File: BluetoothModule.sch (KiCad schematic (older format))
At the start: 15 parts, among them J8 SW_DIP_x01, U17 BM83SM1-00TA

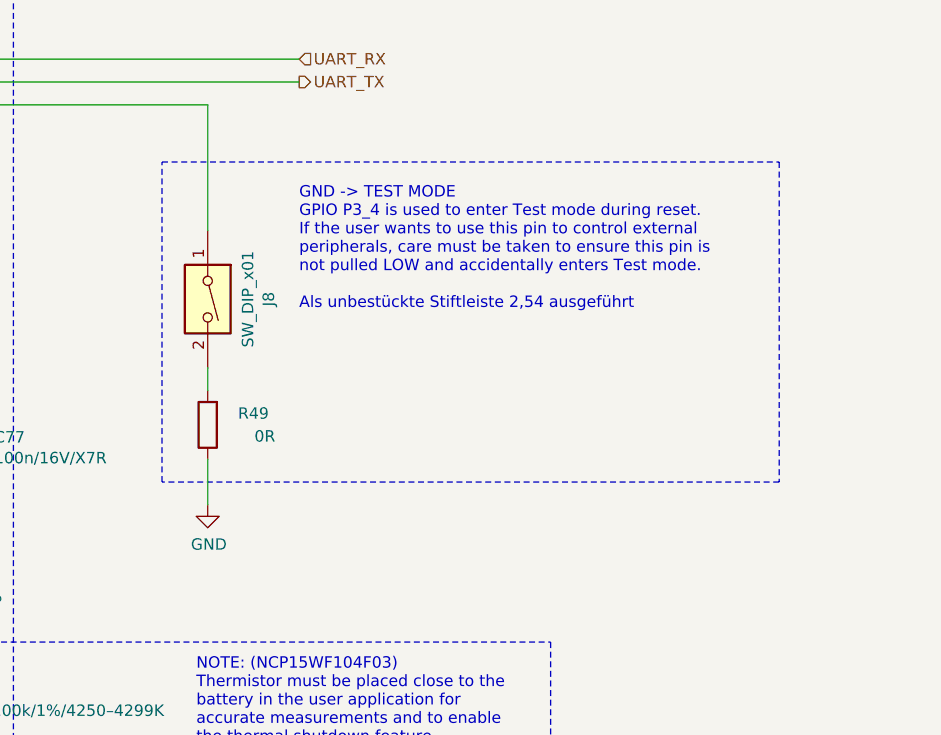
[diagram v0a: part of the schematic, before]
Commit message: - 1,5mm Connector aus BOM gestrichen, damit ist kein Platz für Bauteile unter CM4 - RTC neben das CM4 verschoben, da mit 1,75mm um 0,25mm zu hoch für unterhalb - BT1 von THT auf SMD Typ gewechselt (Beinchen könnten Kurzschluss auf CM4 verursachen)
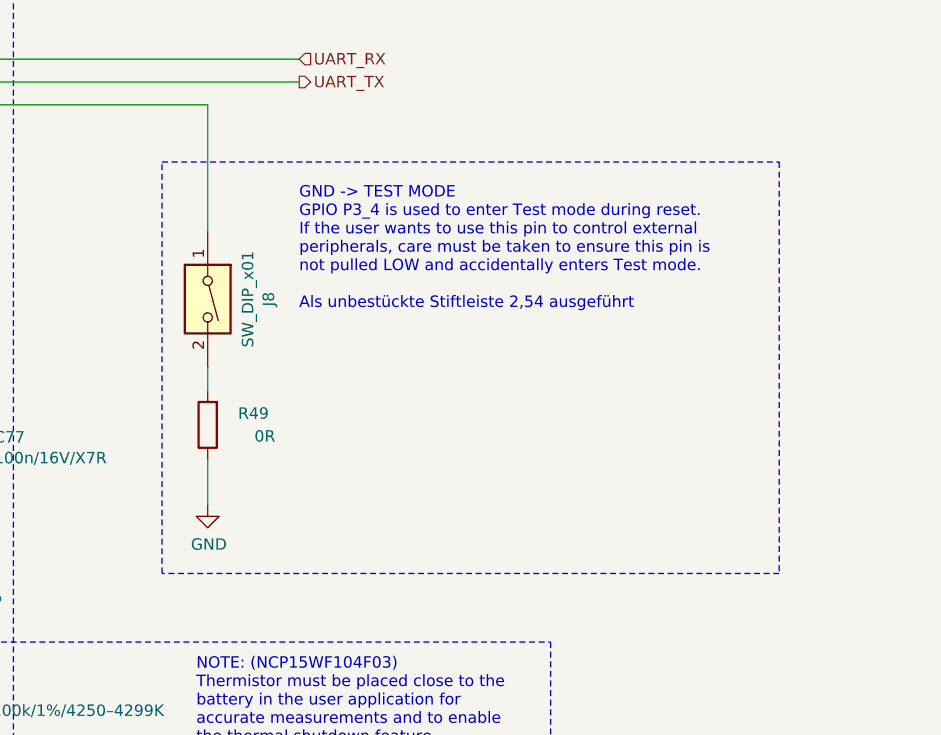
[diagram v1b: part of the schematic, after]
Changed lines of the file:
@@
 	8500 2100 11200 2100
 Wire Notes Line
-	11200 2100 11200 3500
+	11200 2100 11200 3900
 Wire Notes Line
-	11200 3500 8500 3500
+	11200 3900 8500 3900
 Wire Notes Line
-	8500 3500 8500 2100
+	8500 3900 8500 2100
 $EndSCHEMATC

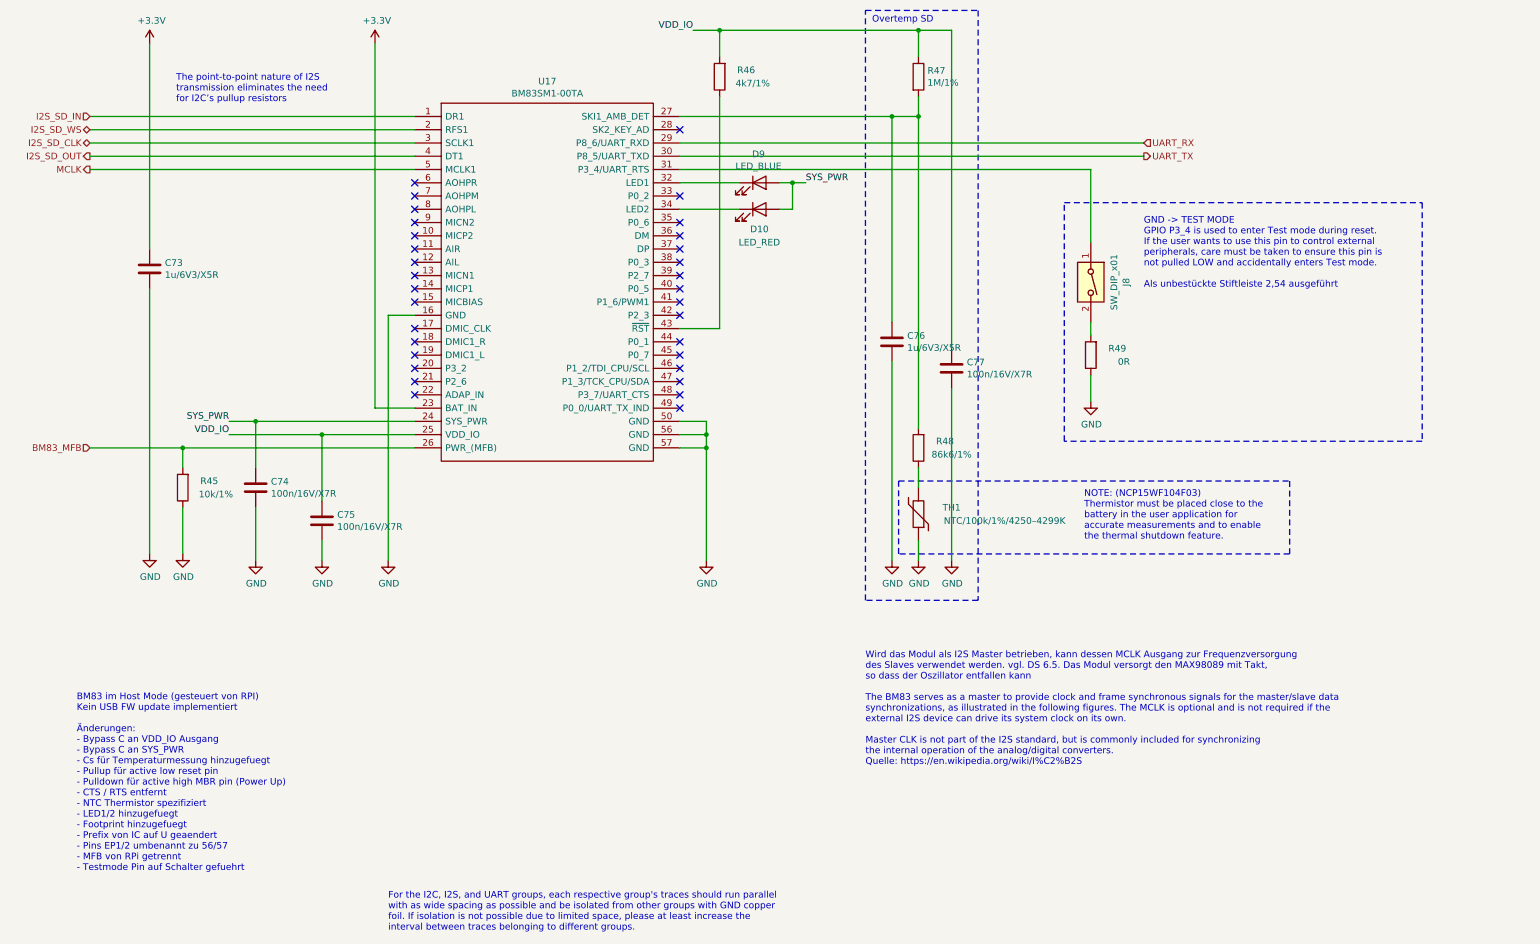
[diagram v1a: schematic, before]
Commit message: - Testpoints für BM83 USB hinzugefuegt
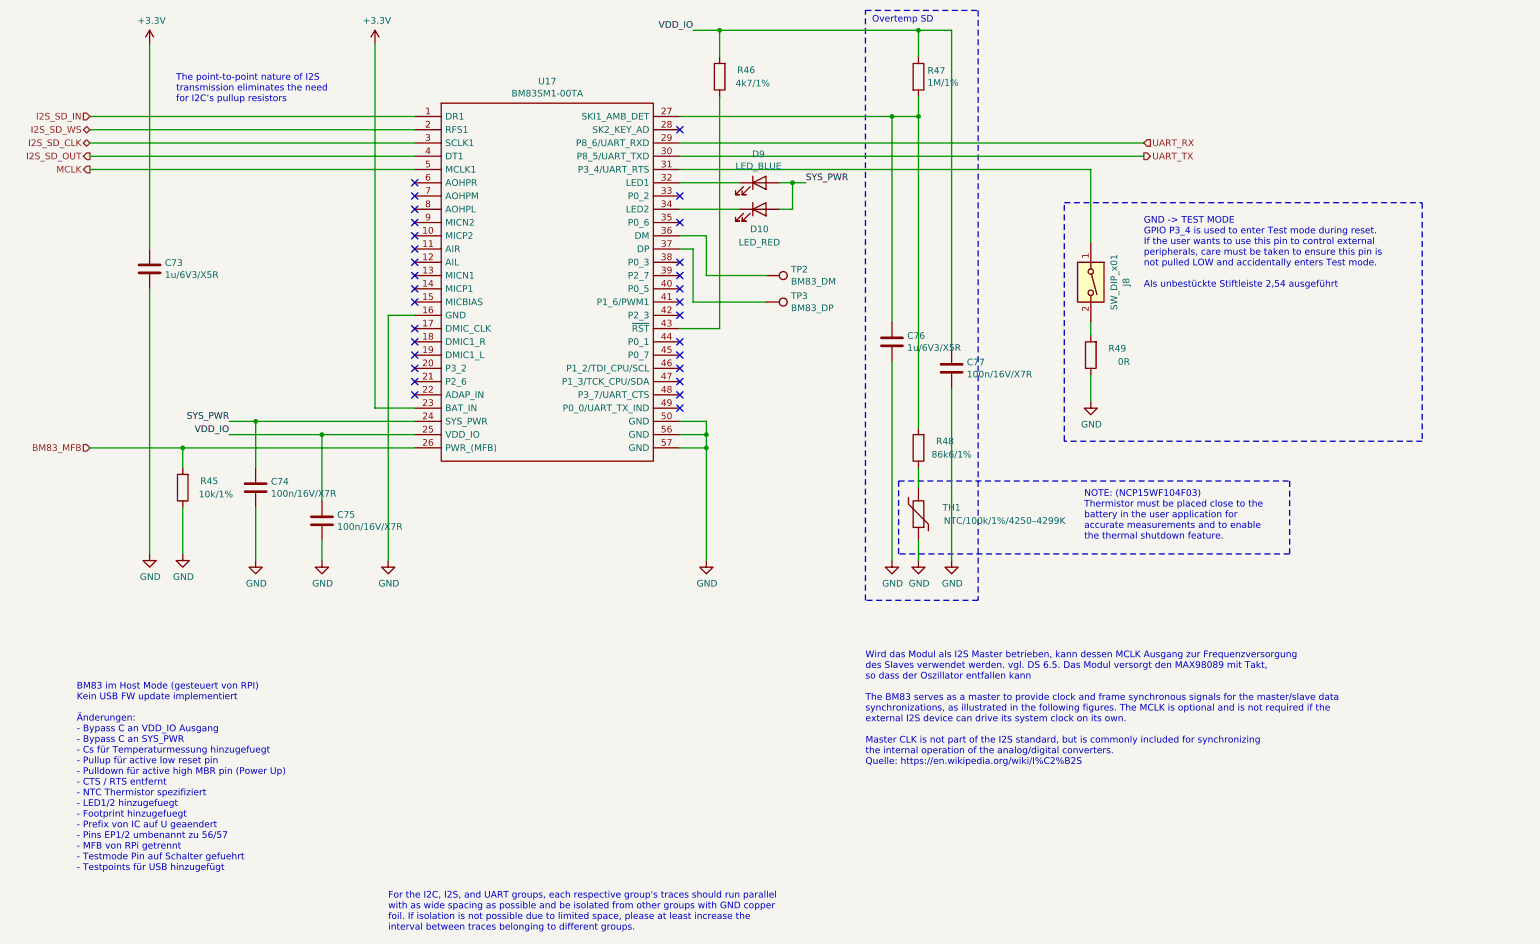
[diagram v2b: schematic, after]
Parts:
- added TP2: BM83_DM, TestPoint:TestPoint_Pad_D1.5mm, symbol Connector:TestPoint
- added TP3: BM83_DP, TestPoint:TestPoint_Pad_D1.5mm, symbol Connector:TestPoint
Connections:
- net at U17.36 (DM): now also TP2.1
- net at U17.37 (DP): now also TP3.1
- no-connect marks 32 -> 30
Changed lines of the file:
@@
 Wire Wire Line
 	3600 3950 1850 3950
-NoConn ~ 5600 2350
-NoConn ~ 5600 2450
 Wire Wire Line
 	5600 3750 5800 3750
@@
 NoConn ~ 5600 3450
 NoConn ~ 5600 2050
-NoConn ~ 5600 2250
 NoConn ~ 5600 2550
 NoConn ~ 5600 2650
@@
 	5800 3850 5800 3950
 Text Notes 1050 7150 0    50   ~ 0
-BM83 im Host Mode (gesteuert von RPI)\nKein USB FW update implementiert\n\nÄnderungen:\n- Bypass C an VDD_IO Ausgang\n- Bypass C an SYS_PWR\n- Cs für Temperaturmessung hinzugefuegt\n- Pullup für active low reset pin\n- Pulldown für active high MBR pin (Power Up)\n- CTS / RTS entfernt\n- NTC Thermistor spezifiziert\n- LED1/2 hinzugefuegt\n- Footprint hinzugefuegt\n- Prefix von IC auf U geaendert\n- Pins EP1/2 umbenannt zu 56/57 \n- MFB von RPi getrennt\n- Testmode Pin auf Schalter gefuehrt
+BM83 im Host Mode (gesteuert von RPI)\nKein USB FW update implementiert\n\nÄnderungen:\n- Bypass C an VDD_IO Ausgang\n- Bypass C an SYS_PWR\n- Cs für Temperaturmessung hinzugefuegt\n- Pullup für active low reset pin\n- Pulldown für active high MBR pin (Power Up)\n- CTS / RTS entfernt\n- NTC Thermistor spezifiziert\n- LED1/2 hinzugefuegt\n- Footprint hinzugefuegt\n- Prefix von IC auf U geaendert\n- Pins EP1/2 umbenannt zu 56/57 \n- MFB von RPi getrennt\n- Testmode Pin auf Schalter gefuehrt\n- Testpoints für USB hinzugefügt
 $Bitmap
 Pos 5150 6250
@@
 Wire Notes Line
 	8500 3900 8500 2100
+NoConn ~ 5600 2250
+$Comp
+L Connector:TestPoint TP2
+U 1 1 61F8CAC4
+P 6250 2650
+F 0 "TP2" V 6204 2838 50  0000 L CNN
+F 1 "BM83_DM" V 6295 2838 50  0000 L CNN
+F 2 "TestPoint:TestPoint_Pad_D1.5mm" H 6450 2650 50  0001 C CNN
+F 3 "~" H 6450 2650 50  0001 C CNN
+	1    6250 2650
+	0    1    1    0
+$EndComp
+$Comp
+L Connector:TestPoint TP3
+U 1 1 61F8F1C2
+P 6250 2850
+F 0 "TP3" V 6204 3038 50  0000 L CNN
+F 1 "BM83_DP" V 6295 3038 50  0000 L CNN
+F 2 "TestPoint:TestPoint_Pad_D1.5mm" H 6450 2850 50  0001 C CNN
+F 3 "~" H 6450 2850 50  0001 C CNN
+	1    6250 2850
+	0    1    1    0
+$EndComp
+Wire Wire Line
+	5600 2350 5800 2350
+Wire Wire Line
+	5800 2350 5800 2650
+Wire Wire Line
+	5800 2650 6250 2650
+Wire Wire Line
+	5600 2450 5700 2450
+Wire Wire Line
+	5700 2450 5700 2850
+Wire Wire Line
+	5700 2850 6250 2850
 $EndSCHEMATC

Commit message: - Reset IC fuer BM83 hinzugefuegt
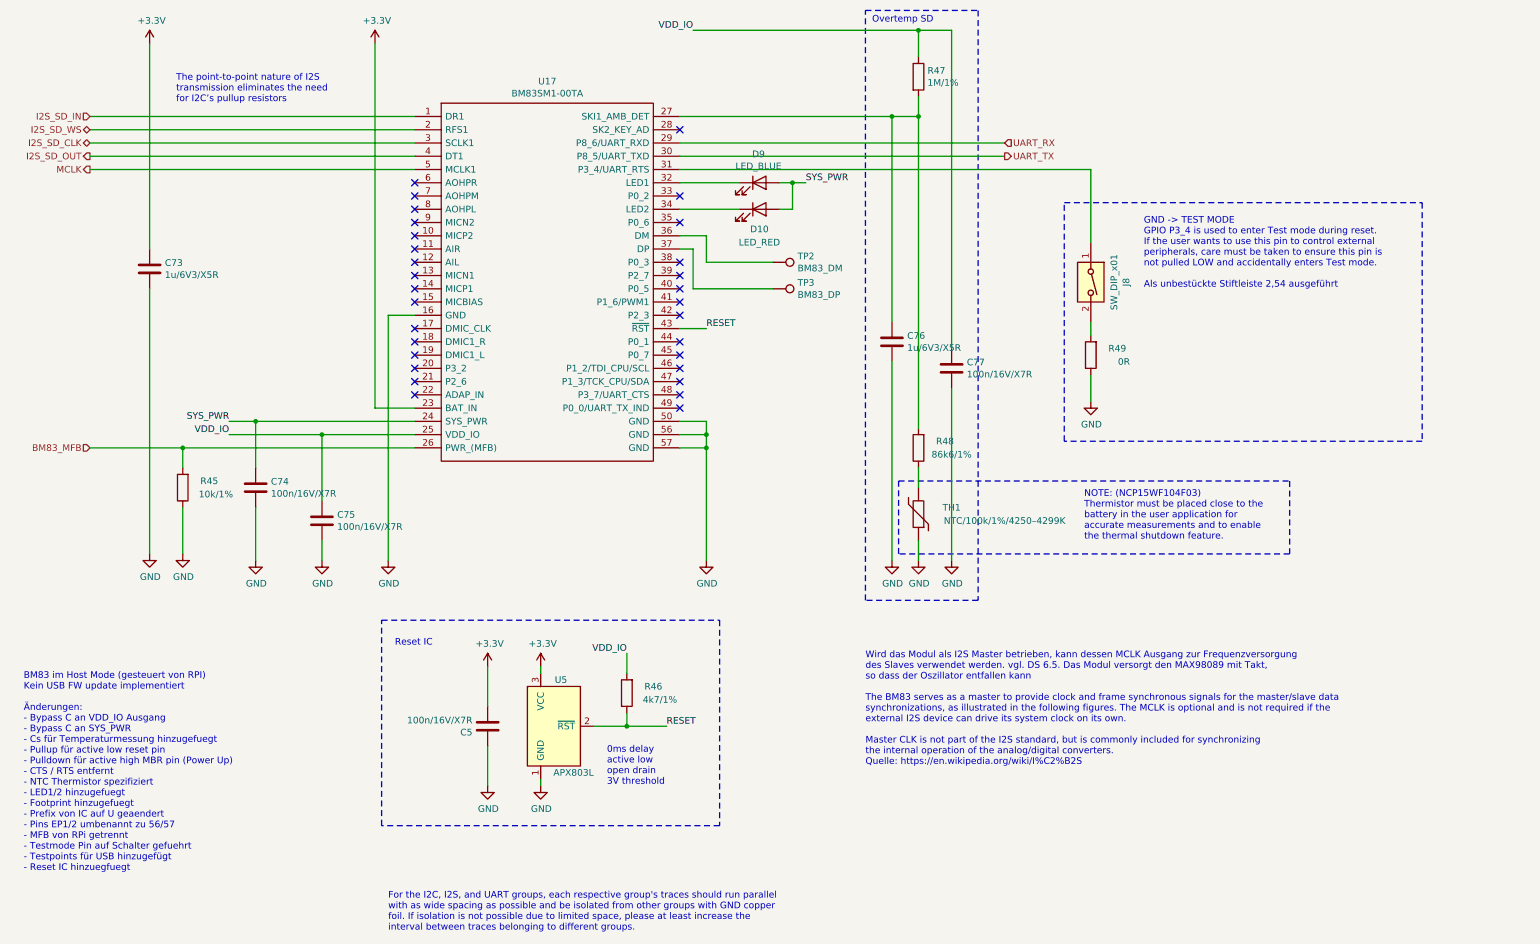
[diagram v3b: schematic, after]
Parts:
- added C5: 100n/16V/X7R, Capacitor_SMD:C_0402_1005Metric, symbol Device:C
- added U5: APX803L, Package_TO_SOT_SMD:SOT-23, symbol TeKaDe:APX803L
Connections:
- net +3V3: now also C5.2, U5.3 (VCC)
- net GND: now also C5.1, U5.1 (GND)
- net RESET: now reaches R46.1, U17.43 (~RST)
- net RESET: now also U5.2 (~RST)
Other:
- note added: "0ms delay\nactive low\nopen drain\n3V threshold"
- note added: "Reset IC"
- moved on the sheet: R46, TP2, TP3

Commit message: - Schaltplan und BOM an BM64 angepasst
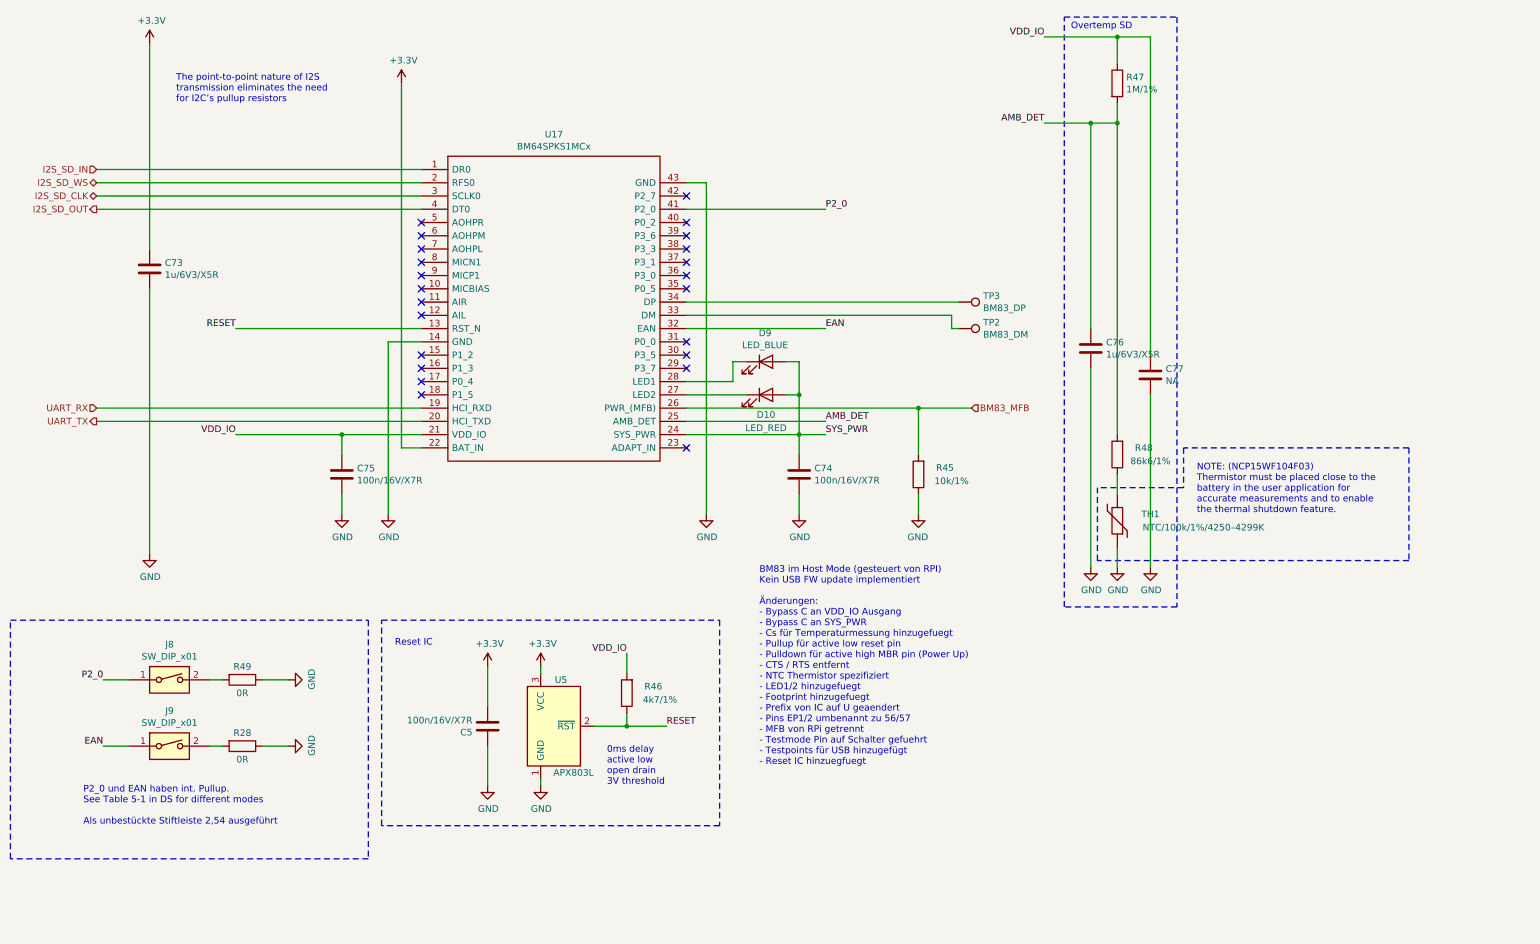
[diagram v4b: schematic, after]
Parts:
- removed U17: BM83SM1-00TA, TeKaDe:BM83SM1, symbol TeKaDe:BM83SM1-00TA
- added J9: SW_DIP_x01, Connector_PinHeader_2.54mm:PinHeader_1x02_P2.54mm_Vertical, symbol Switch:SW_DIP_x01
- added R28: 0R, Resistor_SMD:R_0603_1608Metric, symbol Device:R
- added U17: BM64SPKS1MCx, TeKaDe:BM64, symbol TeKaDe:BM64SPKS1MCx
- C77: value 100n/16V/X7R -> NA
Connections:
- net +3V3: now also U17.22 (BAT_IN)
- net BM83_MFB: now also U17.26 (PWR_(MFB))
- net GND: now also R28.1, U17.14 (GND), U17.43 (GND)
- net I2S_SD_CLK: now also U17.3 (SCLK0)
- net I2S_SD_IN: now also U17.1 (DR0)
- net I2S_SD_OUT: now also U17.4 (DT0)
- net I2S_SD_WS: now also U17.2 (RFS0)
- net RESET: now also U17.13 (RST_N)
- net SYS_PWR: now also U17.24 (SYS_PWR)
- net UART_RX: now also U17.19 (HCI_RXD)
- net UART_TX: now also U17.20 (HCI_TXD)
- net VDD_IO: now also U17.21 (VDD_IO)
- net AMB_DET: now reaches C76.1, R47.2, R48.2
- net AMB_DET: now also U17.25 (AMB_DET)
- net at D9.1 (K): now also U17.28 (LED1)
- net at D10.1 (K): now also U17.27 (LED2)
- net P2_0: now reaches J8.1
- net P2_0: now also U17.41 (P2_0)
- net at TP2.1: now also U17.33 (DM)
- net at TP3.1: now also U17.34 (DP)
- new net: J9.2, R28.2
- new net EAN: J9.1, U17.32 (EAN)
- no-connect marks 30 -> 23
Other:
- note added: "P2_0 und EAN haben int. Pullup.\nSee Table 5-1 in DS for different modes\n\nAls unbestückte Stiftleiste 2,54 ausgeführt"
- note removed: "For the I2C, I2S, and UART groups, each respective group's traces should run parallel\nwith as wide spacing as possible and be isolated from other groups with GND copper\nfoil. If isolation is not possible due to limited space, please at least increase the \ninterval between traces belonging to different groups."
- note removed: "GND -> TEST MODE\nGPIO P3_4 is used to enter Test mode during reset. \nIf the user wants to use this pin to control external\nperipherals, care must be taken to ensure this pin is \nnot pulled LOW and accidentally enters Test mode.\n\nAls unbestückte Stiftleiste 2,54 ausgeführt"
- note removed: "Wird das Modul als I2S Master betrieben, kann dessen MCLK Ausgang zur Frequenzversorgung \ndes Slaves verwendet werden. vgl. DS 6.5. Das Modul versorgt den MAX98089 mit Takt, \nso dass der Oszillator entfallen kann\n\nThe BM83 serves as a master to provide clock and frame synchronous signals for the master/slave data\nsynchronizations, as illustrated in the following figures. The MCLK is optional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"
- moved on the sheet: C74, C75, C76, C77, D10, D9, J8, R45, R47, R48, R49, TH1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

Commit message: [add:] annotations, corrections from testing
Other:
- note added: "ADAPT_IN an 5V -> einfacheres flashen per USB"
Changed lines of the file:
@@
 Data
 89 50 4E 47 0D 0A 1A 0A 00 00 00 0D 49 48 44 52 00 00 05 D7 00 00 02 9F 08 02 00 00 00 03 DC 66
-88 00 00 00 03 73 42 49 54 08 08 08 DB E1 4F E0 00 00 00 09 70 48 59 73 00 00 19 D6 00 00 19 D6
-01 18 D1 CA ED 00 00 20 00 49 44 41 54 78 9C EC 9D 79 B4 65 55 75 EE BF D5 ED E6 34 B7 A9 AA 5B
+88 00 00 00 03 73 42 49 54 08 08 08 DB E1 4F E0 00 00 00 09 70 48 59 73 00 00 19 C8 00 00 19 C8
+01 F5 4C 96 D9 00 00 20 00 49 44 41 54 78 9C EC 9D 79 B4 65 55 75 EE BF D5 ED E6 34 B7 A9 AA 5B
 45 53 20 28 3D F6 B4 F6 82 44 11 44 C4 D8 12 8D 31 B6 B1 4B 24 EA 88 26 1A 9B 3C 21 1A 62 8B 8A
 02 2A 18 14 45 44 11 95 C4 5E 04 D4 A0 B4 A2 02 45 41 59 50 54 DD 5B F7 DE D3 EC BD 57 37 E7 FB
@@
 EndData
 $EndBitmap
+Text Notes 4400 4150 0    50   ~ 0
+ADAPT_IN an 5V -> einfacheres flashen per USB
 $EndSCHEMATC
